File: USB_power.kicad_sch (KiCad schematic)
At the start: 22 parts, among them J1 JST-4-pin, J1 TYPE-C-31-M12_13, SW1 MK-12C02-G025, U1 BQ24074RGTR, U4 TPD4E05U06DQAR

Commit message: Finalized hardware Ver 1 release
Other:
- company: (none) -> HW-tinkerers
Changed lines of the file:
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@@
   (title_block
     (title "USB and Power Path ")
-    (date "2023-06-05")
+    (date "2024-02-17")
     (rev "1.0")
+    (company "HW-tinkerers")
   )
   (junction (at 39.37 115.57) (diameter 0) (color 0 0 0 0)

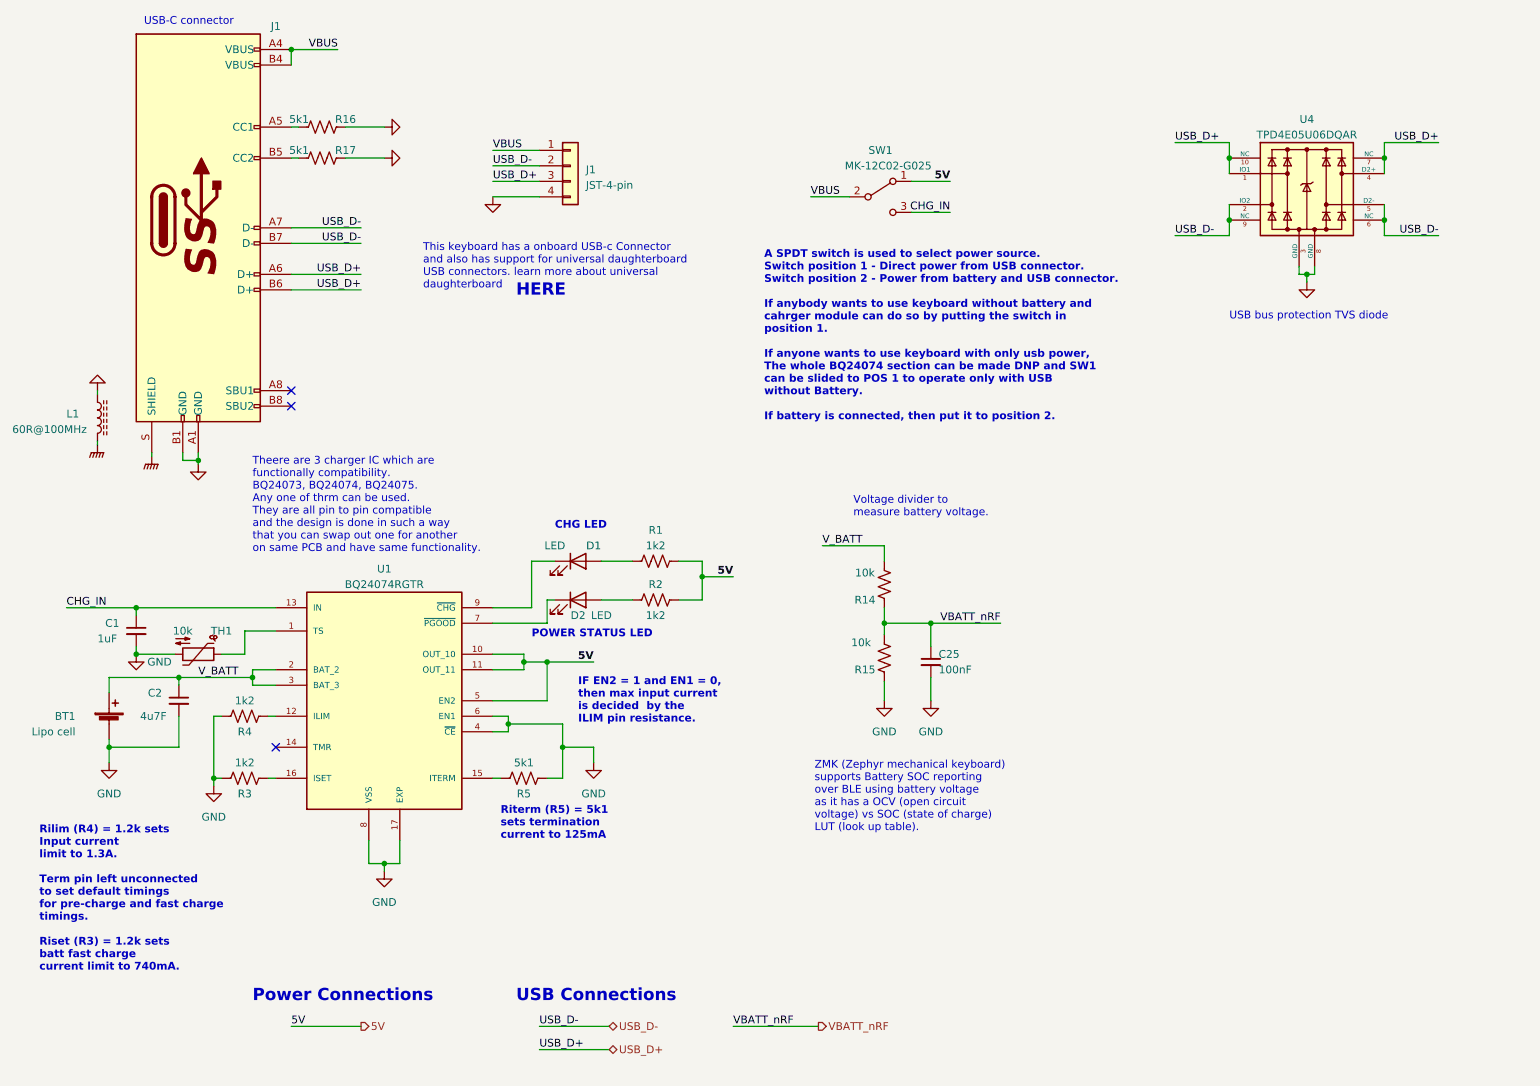
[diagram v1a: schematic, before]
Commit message: Exported edge cuts as footprint and set grid origin
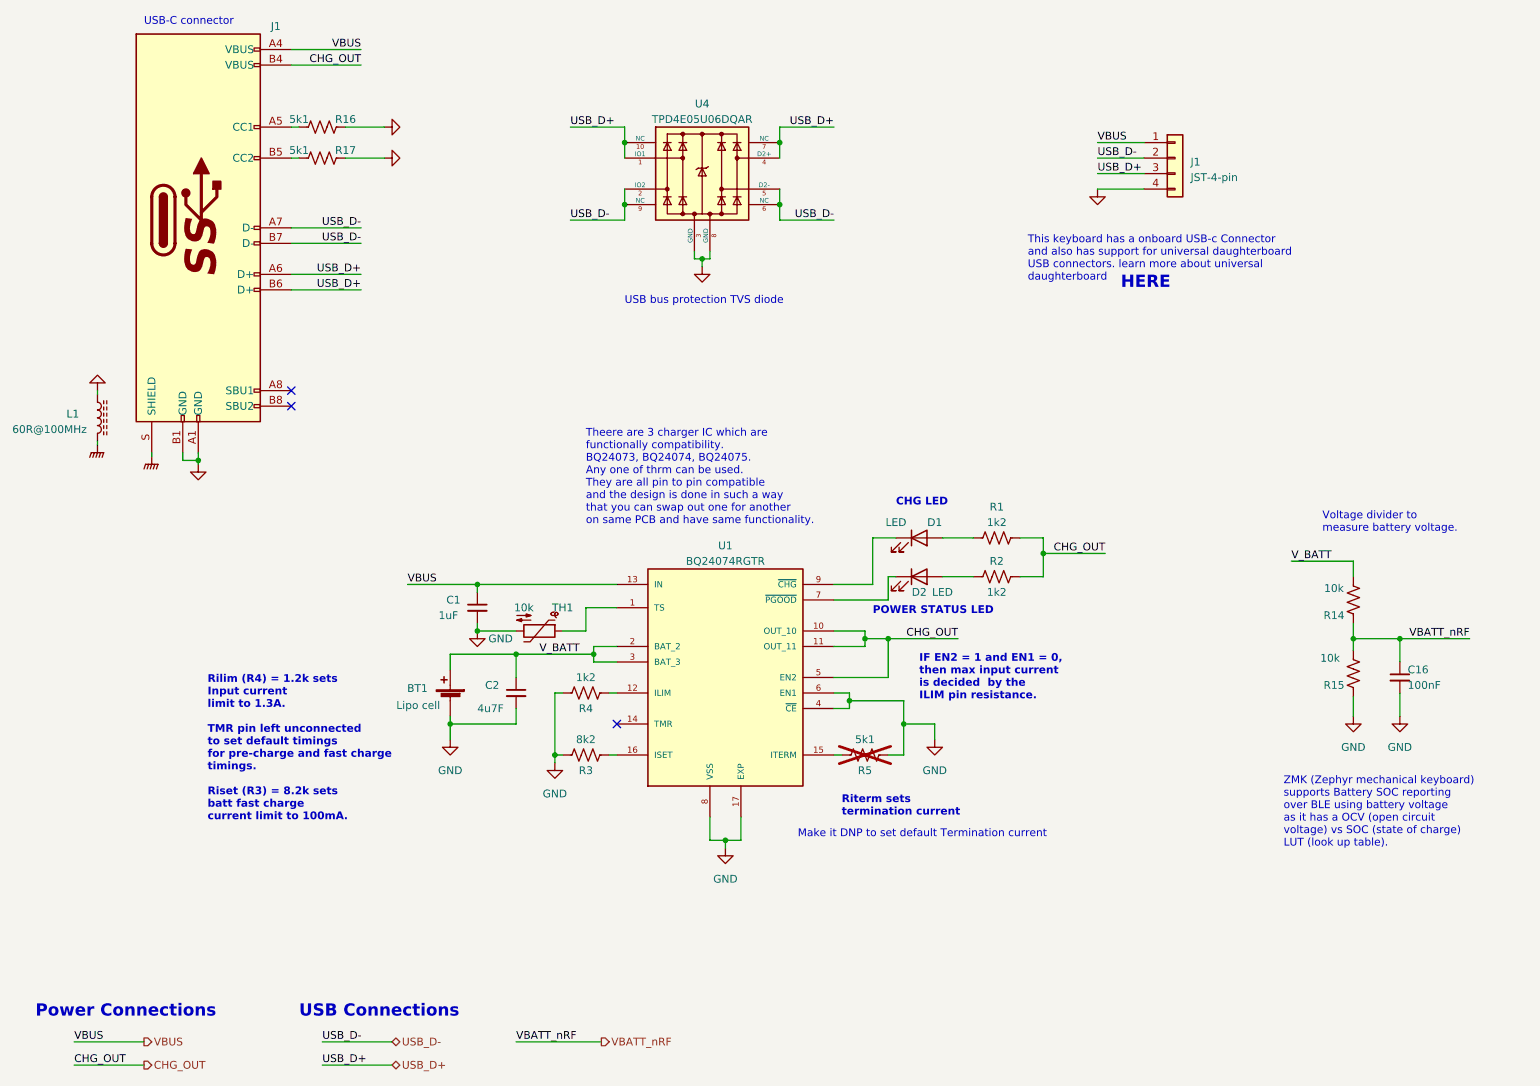
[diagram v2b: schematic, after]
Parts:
- removed SW1: MK-12C02-G025, keyboard:SPDT, symbol keyboard:SW_SPDT
- BT1: LCSC Part Number C160402 -> C295747; LCSC link https://www.lcsc.com/product-detail/Wire-To-Board-Wire-To-W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 -> https://www.lcsc.com/product-detail/Wire-To-Board-Connector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; PN SM02B-SRSS-TB(LF)(SN) -> JST S2B-PH-SM4-TB(LF)(SN)
- R3: value 1k2 -> 8k2; LCSC Part Number C138040 -> C170361; LCSC link https://www.lcsc.com/product-detail/Chip-Resistor-Surface-Mount_YAGEO-RC0402FR-071K2L_C138040.html -> https://www.lcsc.com/product-detail/Chip-Resistor-Surface-Mount_Walsin-Tech-Corp-WR04X8201FTL_C170361.html; PN RC0402FR-071K2L -> WR04X8201FTL
- R5: now not fitted; now left out of the parts list
- renumbered C25 to C16
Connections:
- net CHG_IN is gone; now on net VBUS: C1.1, U1.13 (IN)
- net VBUS: no longer J1.B4 (VBUS)
- net 5V renamed CHG_OUT
- net CHG_OUT: now also J1.B4 (VBUS)
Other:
- note added: "Make it DNP to set default Termination current"
- note added: "Rilim (R4) = 1.2k sets Input current limit to 1.3A. TMR pin left unconnected to set default timings for pre-charge and fast charge timings. Riset (R3) = 8.2k sets batt fast charge current limit to 100mA."
- note added: "Riterm sets termination current"
- note removed: "A SPDT switch is used to select power source. Switch position 1 - Direct power from USB connector. Switch position 2 - Power from battery and USB connector. If anybody wants to use keyboard without battery and cahrger module can do so by putting the switch in position 1. If anyone wants to use keyboard with only usb power, The whole BQ24074 section can be made DNP and SW1 can be slided to POS 1 t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"
- note removed: "Rilim (R4) = 1.2k sets Input current limit to 1.3A. Term pin left unconnected to set default timings for pre-charge and fast charge timings. Riset (R3) = 1.2k sets batt fast charge current limit to 740mA."
- note removed: "Riterm (R5) = 5k1 sets termination current to 125mA"
- moved on the sheet: BT1, C1, C16, C2, D1, D2, J1, R1, R14, R15, R2, R3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
